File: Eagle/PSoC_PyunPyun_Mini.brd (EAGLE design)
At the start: 57.1 x 52.1 mm, 26 parts, among them IC1 NJM2732

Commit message: change Bord Design
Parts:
- moved R3 2.54 mm to (33.0, 16.5)
- moved JP9 2.54 mm to (38.1, 22.9)
- moved R5 2.54 mm to (29.2, 10.2)
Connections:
- net IDAC7: now also JP3.9; no longer JP3.8
- net IDAC8: now also JP3.8; no longer JP3.9
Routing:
- net AGND: track 65.6 -> 72.2 mm
- net +3.3V: track 44.8 -> 50.8 mm
- net GND: track 93.5 -> 88.9 mm
- net +5V: track 56.4 -> 61.0 mm
- net RST: track 32.6 -> 35.6 mm
- net N$2: track 25.0 -> 27.9 mm
- net N$1: track 12.7 -> 10.2 mm
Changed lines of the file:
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@@
 <element name="R13" library="rcl" package="0207/7" value="1k" x="44.45" y="35.56"/>
 <element name="R2" library="rcl" package="0207/7" value="33k" x="27.94" y="16.51" rot="R90"/>
-<element name="R3" library="rcl" package="0207/7" value="2.2k" x="33.02" y="13.97" rot="R270"/>
+<element name="R3" library="rcl" package="0207/7" value="2.2k" x="33.02" y="16.51" rot="R270"/>
 <element name="R4" library="rcl" package="0207/7" value="10k" x="15.24" y="26.67" rot="R90"/>
 <element name="R9" library="rcl" package="0207/7" value="10k" x="27.94" y="36.83" rot="R90"/>
@@
 <element name="IC1" library="linear" package="DIL08" value="NJM2732" x="24.13" y="26.67"/>
 <element name="JP7" library="pinhead" package="1X02" value="RCA_GND" x="13.97" y="20.32" rot="R180"/>
-<element name="R5" library="rcl" package="0207/7" value="10k" x="26.67" y="10.16" rot="R180"/>
+<element name="R5" library="rcl" package="0207/7" value="10k" x="29.21" y="10.16" rot="R180"/>
 <element name="C4" library="rcl" package="C050-024X044" value="1500pF" x="30.48" y="15.24" rot="R90"/>
 <element name="JP8" library="pinhead" package="1X01" value="TP-VGND" x="15.24" y="15.24" rot="R180"/>
-<element name="JP9" library="pinhead" package="1X01" value="TP-GND" x="38.1" y="20.32"/>
+<element name="JP9" library="pinhead" package="1X01" value="TP-GND" x="38.1" y="22.86"/>
 <element name="JP4" library="pinhead" package="1X09" value="" x="50.8" y="25.4" rot="R90"/>
 </elements>
@@
 <contactref element="R2" pad="1"/>
 <contactref element="C2" pad="1"/>
-<wire x1="20.32" y1="12.7" x2="20.32" y2="15.24" width="0.4064" layer="16"/>
-<wire x1="20.32" y1="15.24" x2="22.86" y2="15.24" width="0.4064" layer="16"/>
 <wire x1="22.86" y1="15.24" x2="22.86" y2="12.7" width="0.4064" layer="16"/>
 <wire x1="22.86" y1="12.7" x2="27.94" y2="12.7" width="0.4064" layer="16"/>
+<wire x1="20.32" y1="12.7" x2="22.86" y2="12.7" width="0.4064" layer="16"/>
 </signal>
 <signal name="IDAC8">
-<contactref element="JP3" pad="9"/>
 <contactref element="R5" pad="1"/>
 <contactref element="R3" pad="2"/>
-<wire x1="33.02" y1="10.16" x2="30.48" y2="10.16" width="0.4064" layer="16"/>
-<wire x1="30.48" y1="10.16" x2="30.48" y2="5.08" width="0.4064" layer="16"/>
+<wire x1="33.02" y1="12.7" x2="33.02" y2="10.16" width="0.4064" layer="16"/>
+<contactref element="JP3" pad="8"/>
+<wire x1="33.02" y1="5.08" x2="33.02" y2="10.16" width="0.4064" layer="16"/>
 </signal>
 <signal name="N$3">
@@
 <wire x1="27.94" y1="22.86" x2="30.48" y2="22.86" width="0.4064" layer="16"/>
 <wire x1="25.4" y1="48.26" x2="25.4" y2="35.56" width="0.4064" layer="16"/>
-<wire x1="35.56" y1="35.56" x2="38.1" y2="33.02" width="0.4064" layer="16"/>
-<wire x1="38.1" y1="33.02" x2="38.1" y2="20.32" width="0.4064" layer="16"/>
+<wire x1="38.1" y1="35.56" x2="38.1" y2="22.86" width="0.4064" layer="16"/>
 <wire x1="25.4" y1="35.56" x2="35.56" y2="35.56" width="0.4064" layer="16"/>
-<wire x1="30.48" y1="22.86" x2="33.02" y2="20.32" width="0.4064" layer="16"/>
-<wire x1="33.02" y1="20.32" x2="38.1" y2="20.32" width="0.4064" layer="16"/>
 <contactref element="JP4" pad="4"/>
 <contactref element="JP4" pad="8"/>
 <wire x1="50.8" y1="33.02" x2="43.18" y2="33.02" width="0.4064" layer="16"/>
-<wire x1="43.18" y1="33.02" x2="43.18" y2="20.32" width="0.4064" layer="16"/>
-<wire x1="43.18" y1="20.32" x2="38.1" y2="20.32" width="0.4064" layer="16"/>
+<wire x1="43.18" y1="33.02" x2="43.18" y2="22.86" width="0.4064" layer="16"/>
+<wire x1="43.18" y1="22.86" x2="38.1" y2="22.86" width="0.4064" layer="16"/>
 <wire x1="50.8" y1="22.86" x2="54.61" y2="22.86" width="0.4064" layer="1"/>
 <wire x1="54.61" y1="22.86" x2="54.61" y2="33.02" width="0.4064" layer="1"/>
 <wire x1="54.61" y1="33.02" x2="50.8" y2="33.02" width="0.4064" layer="1"/>
+<wire x1="30.48" y1="22.86" x2="38.1" y2="22.86" width="0.4064" layer="16"/>
+<wire x1="35.56" y1="35.56" x2="38.1" y2="35.56" width="0.4064" layer="16"/>
 </signal>
 <signal name="N$8">
@@
 <contactref element="IC1" pad="8"/>
 <wire x1="17.78" y1="30.48" x2="20.32" y2="30.48" width="0.4064" layer="16"/>
-<wire x1="35.56" y1="25.4" x2="24.13" y2="25.4" width="0.4064" layer="1"/>
-<wire x1="24.13" y1="25.4" x2="20.32" y2="29.21" width="0.4064" layer="1"/>
-<wire x1="20.32" y1="29.21" x2="20.32" y2="30.48" width="0.4064" layer="1"/>
-<wire x1="20.32" y1="30.48" x2="20.32" y2="33.02" width="0.4064" layer="1"/>
-<wire x1="20.32" y1="33.02" x2="27.94" y2="40.64" width="0.4064" layer="1"/>
-<wire x1="40.64" y1="35.56" x2="35.56" y2="40.64" width="0.4064" layer="16"/>
-<wire x1="35.56" y1="40.64" x2="30.48" y2="40.64" width="0.4064" layer="16"/>
+<wire x1="40.64" y1="35.56" x2="40.64" y2="40.64" width="0.4064" layer="16"/>
+<wire x1="40.64" y1="40.64" x2="30.48" y2="40.64" width="0.4064" layer="16"/>
 <wire x1="30.48" y1="40.64" x2="27.94" y2="40.64" width="0.4064" layer="16"/>
 <wire x1="30.48" y1="48.26" x2="30.48" y2="40.64" width="0.4064" layer="16"/>
+<wire x1="27.94" y1="40.64" x2="20.32" y2="40.64" width="0.4064" layer="1"/>
+<wire x1="20.32" y1="40.64" x2="20.32" y2="30.48" width="0.4064" layer="1"/>
+<wire x1="35.56" y1="25.4" x2="40.64" y2="25.4" width="0.4064" layer="1"/>
+<wire x1="40.64" y1="25.4" x2="40.64" y2="35.56" width="0.4064" layer="1"/>
 </signal>
 <signal name="AGND">
@@
 <wire x1="15.24" y1="22.86" x2="15.24" y2="20.32" width="0.4064" layer="16"/>
 <wire x1="25.4" y1="30.48" x2="22.86" y2="30.48" width="0.4064" layer="16"/>
-<wire x1="33.02" y1="17.78" x2="30.48" y2="17.78" width="0.4064" layer="16"/>
 <wire x1="15.24" y1="15.24" x2="16.51" y2="16.51" width="0.4064" layer="1"/>
 <wire x1="16.51" y1="16.51" x2="24.13" y2="16.51" width="0.4064" layer="1"/>
 <wire x1="24.13" y1="16.51" x2="25.4" y2="15.24" width="0.4064" layer="1"/>
 <wire x1="15.24" y1="20.32" x2="15.24" y2="15.24" width="0.4064" layer="16"/>
-<wire x1="25.4" y1="15.24" x2="27.94" y2="17.78" width="0.4064" layer="16"/>
-<wire x1="27.94" y1="17.78" x2="30.48" y2="17.78" width="0.4064" layer="16"/>
 <wire x1="15.24" y1="22.86" x2="15.24" y2="25.4" width="0.4064" layer="16"/>
 <wire x1="15.24" y1="25.4" x2="15.24" y2="27.94" width="0.4064" layer="16"/>
@@
 <wire x1="35.56" y1="27.94" x2="30.48" y2="27.94" width="0.4064" layer="16"/>
 <wire x1="35.56" y1="27.94" x2="35.56" y2="33.02" width="0.4064" layer="16"/>
+<wire x1="25.4" y1="15.24" x2="33.02" y2="15.24" width="0.4064" layer="16"/>
+<wire x1="33.02" y1="15.24" x2="33.02" y2="17.78" width="0.4064" layer="16"/>
+<wire x1="33.02" y1="17.78" x2="33.02" y2="20.32" width="0.4064" layer="16"/>
+<wire x1="30.48" y1="17.78" x2="33.02" y2="17.78" width="0.4064" layer="16"/>
 </signal>
 <signal name="+3.3V">
 <contactref element="JP1" pad="4"/>
 <contactref element="JP4" pad="1"/>
-<wire x1="50.8" y1="15.24" x2="43.18" y2="15.24" width="0.4064" layer="1"/>
-<wire x1="43.18" y1="15.24" x2="40.64" y2="17.78" width="0.4064" layer="1"/>
-<wire x1="33.02" y1="48.26" x2="33.02" y2="40.64" width="0.4064" layer="1"/>
-<wire x1="33.02" y1="40.64" x2="40.64" y2="33.02" width="0.4064" layer="1"/>
-<wire x1="40.64" y1="33.02" x2="40.64" y2="17.78" width="0.4064" layer="1"/>
+<wire x1="50.8" y1="15.24" x2="46.99" y2="15.24" width="0.4064" layer="1"/>
+<wire x1="46.99" y1="15.24" x2="46.99" y2="41.91" width="0.4064" layer="1"/>
+<wire x1="46.99" y1="41.91" x2="33.02" y2="41.91" width="0.4064" layer="1"/>
+<wire x1="33.02" y1="41.91" x2="33.02" y2="48.26" width="0.4064" layer="1"/>
 </signal>
 <signal name="RST">
 <contactref element="JP3" pad="5"/>
 <contactref element="JP4" pad="7"/>
-<wire x1="40.64" y1="5.08" x2="40.64" y2="12.7" width="0.4064" layer="16"/>
-<wire x1="40.64" y1="12.7" x2="45.72" y2="17.78" width="0.4064" layer="16"/>
-<wire x1="45.72" y1="17.78" x2="45.72" y2="30.48" width="0.4064" layer="16"/>
+<wire x1="40.64" y1="5.08" x2="40.64" y2="20.32" width="0.4064" layer="16"/>
+<wire x1="40.64" y1="20.32" x2="45.72" y2="20.32" width="0.4064" layer="16"/>
+<wire x1="45.72" y1="20.32" x2="45.72" y2="30.48" width="0.4064" layer="16"/>
 <wire x1="45.72" y1="30.48" x2="50.8" y2="30.48" width="0.4064" layer="16"/>
 </signal>
@@
 <contactref element="R1" pad="1"/>
 <contactref element="C4" pad="1"/>
-<wire x1="20.32" y1="20.32" x2="17.78" y2="17.78" width="0.4064" layer="16"/>
-<wire x1="17.78" y1="17.78" x2="17.78" y2="10.16" width="0.4064" layer="16"/>
-<wire x1="17.78" y1="10.16" x2="22.86" y2="10.16" width="0.4064" layer="16"/>
-<wire x1="30.48" y1="12.7" x2="27.94" y2="10.16" width="0.4064" layer="16"/>
-<wire x1="27.94" y1="10.16" x2="22.86" y2="10.16" width="0.4064" layer="16"/>
+<wire x1="25.4" y1="10.16" x2="17.78" y2="10.16" width="0.4064" layer="16"/>
+<wire x1="17.78" y1="10.16" x2="17.78" y2="20.32" width="0.4064" layer="16"/>
+<wire x1="17.78" y1="20.32" x2="20.32" y2="20.32" width="0.4064" layer="16"/>
+<wire x1="25.4" y1="10.16" x2="30.48" y2="10.16" width="0.4064" layer="16"/>
+<wire x1="30.48" y1="10.16" x2="30.48" y2="12.7" width="0.4064" layer="16"/>
 </signal>
 <signal name="IDAC7">
-<contactref element="JP3" pad="8"/>
+<contactref element="JP3" pad="9"/>
 </signal>
 </signals>

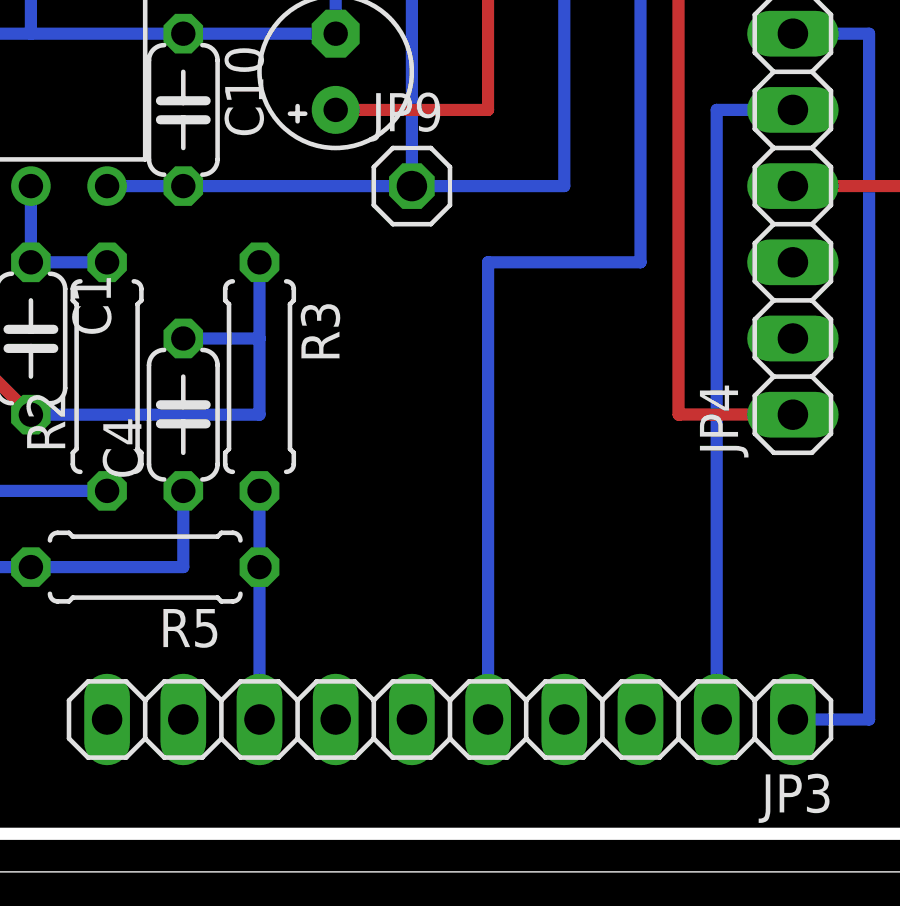
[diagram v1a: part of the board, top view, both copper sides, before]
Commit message: 回路図・基板図 RST信号に抵抗分圧を追加
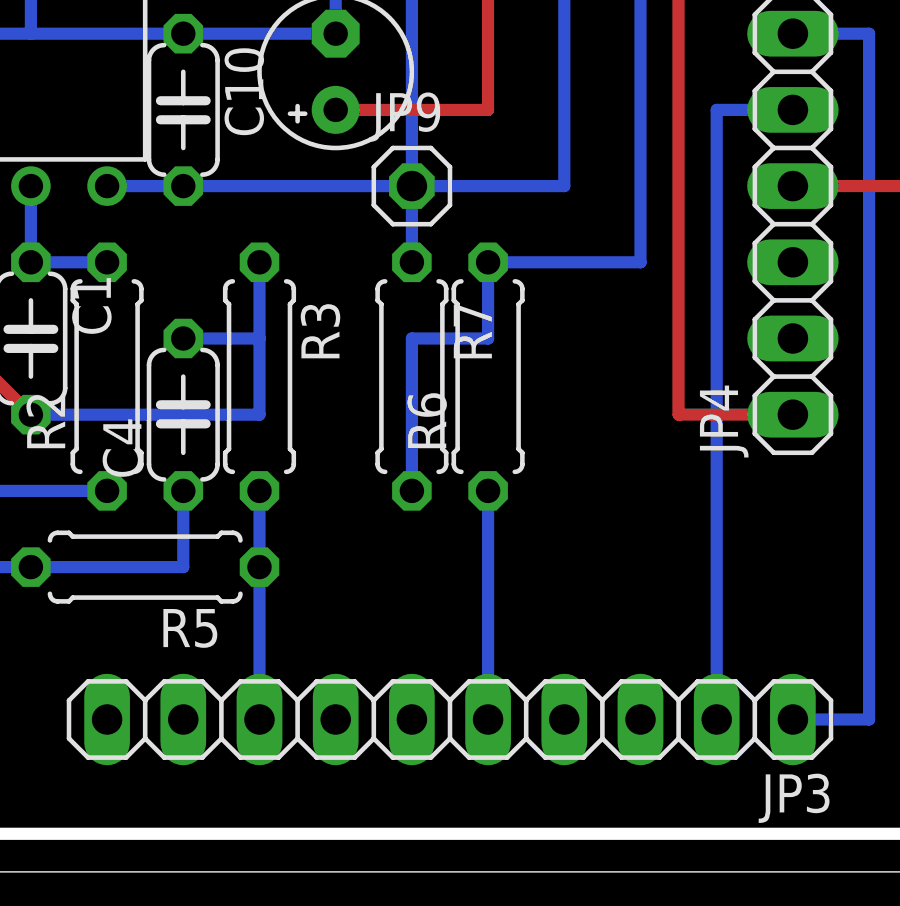
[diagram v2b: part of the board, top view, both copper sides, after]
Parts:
- added R6: 1.2k, rcl:0207/7
- added R7: 2.2k, rcl:0207/7
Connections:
- new net N$6: JP3.5, R6.1
- net GND: now also R7.1
- net RST: now also R6.2, R7.2; no longer JP3.5
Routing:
- net N$6: track 0.00 -> 7.62 mm
- net RST: track 35.6 -> 30.5 mm
- net GND: track 88.9 -> 91.4 mm
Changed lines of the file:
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@@
 <element name="JP9" library="pinhead" package="1X01" value="TP-GND" x="38.1" y="22.86"/>
 <element name="JP4" library="pinhead" package="1X09" value="" x="50.8" y="25.4" rot="R90"/>
+<element name="R6" library="rcl" package="0207/7" value="1.2k" x="40.64" y="16.51" rot="R90"/>
+<element name="R7" library="rcl" package="0207/7" value="2.2k" x="38.1" y="16.51" rot="R270"/>
 </elements>
 <signals>
@@
 <wire x1="30.48" y1="22.86" x2="38.1" y2="22.86" width="0.4064" layer="16"/>
 <wire x1="35.56" y1="35.56" x2="38.1" y2="35.56" width="0.4064" layer="16"/>
+<contactref element="R7" pad="1"/>
+<wire x1="38.1" y1="20.32" x2="38.1" y2="22.86" width="0.4064" layer="16"/>
 </signal>
 <signal name="N$8">
@@
 </signal>
 <signal name="RST">
-<contactref element="JP3" pad="5"/>
 <contactref element="JP4" pad="7"/>
-<wire x1="40.64" y1="5.08" x2="40.64" y2="20.32" width="0.4064" layer="16"/>
-<wire x1="40.64" y1="20.32" x2="45.72" y2="20.32" width="0.4064" layer="16"/>
 <wire x1="45.72" y1="20.32" x2="45.72" y2="30.48" width="0.4064" layer="16"/>
 <wire x1="45.72" y1="30.48" x2="50.8" y2="30.48" width="0.4064" layer="16"/>
+<contactref element="R6" pad="2"/>
+<contactref element="R7" pad="2"/>
+<wire x1="40.64" y1="20.32" x2="45.72" y2="20.32" width="0.4064" layer="16"/>
+<wire x1="38.1" y1="12.7" x2="38.1" y2="17.78" width="0.4064" layer="16"/>
+<wire x1="38.1" y1="17.78" x2="40.64" y2="17.78" width="0.4064" layer="16"/>
+<wire x1="40.64" y1="17.78" x2="40.64" y2="20.32" width="0.4064" layer="16"/>
 </signal>
 <signal name="SCL">
@@
 <contactref element="JP3" pad="9"/>
 </signal>
+<signal name="N$6">
+<contactref element="JP3" pad="5"/>
+<contactref element="R6" pad="1"/>
+<wire x1="40.64" y1="12.7" x2="40.64" y2="5.08" width="0.4064" layer="16"/>
+</signal>
 </signals>

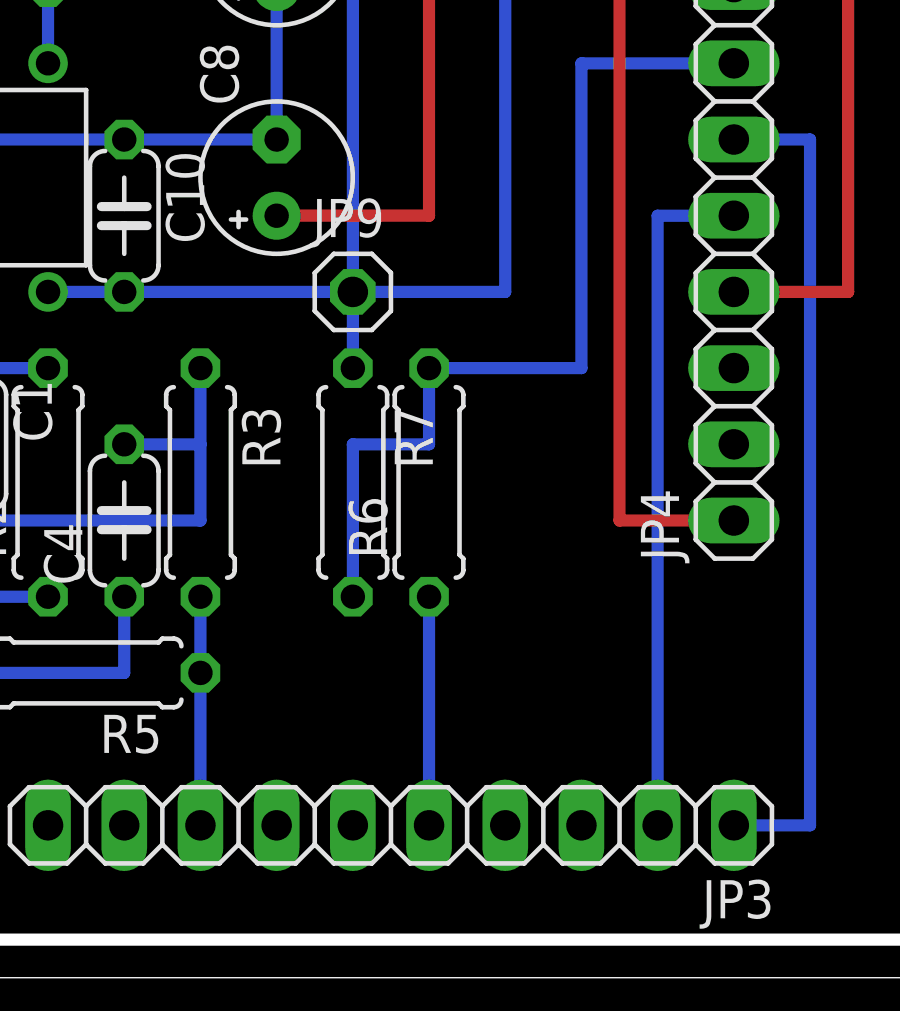
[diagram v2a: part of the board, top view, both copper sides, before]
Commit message: 基板設計図 RST信号の分圧抵抗の位置を変更
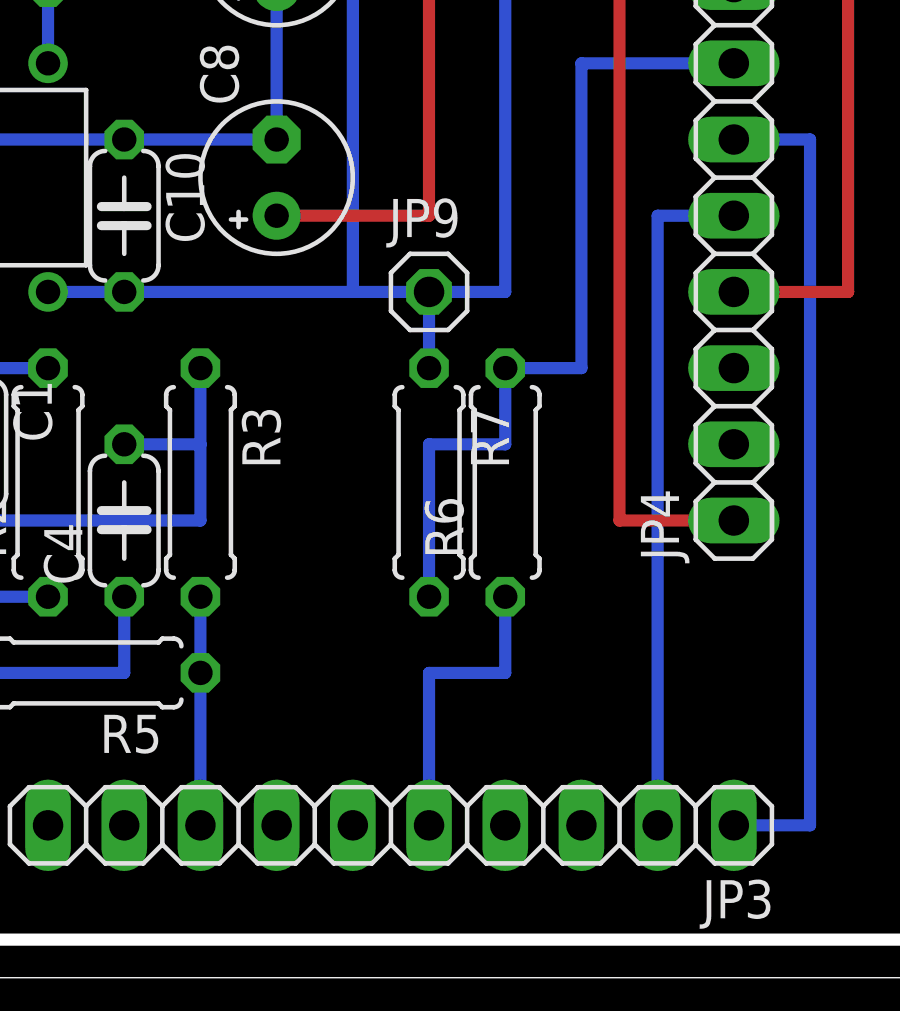
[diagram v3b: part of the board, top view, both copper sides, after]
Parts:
- moved JP9 2.54 mm to (40.6, 22.9)
- moved R6 2.54 mm to (43.2, 16.5)
- moved R7 2.54 mm to (40.6, 16.5)
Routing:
- net RST: track 30.5 -> 27.9 mm
- net N$6: track 7.62 -> 10.2 mm
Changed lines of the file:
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@@
 <element name="C4" library="rcl" package="C050-024X044" value="1500pF" x="30.48" y="15.24" rot="R90"/>
 <element name="JP8" library="pinhead" package="1X01" value="TP-VGND" x="15.24" y="15.24" rot="R180"/>
-<element name="JP9" library="pinhead" package="1X01" value="TP-GND" x="38.1" y="22.86"/>
+<element name="JP9" library="pinhead" package="1X01" value="TP-GND" x="40.64" y="22.86"/>
 <element name="JP4" library="pinhead" package="1X09" value="" x="50.8" y="25.4" rot="R90"/>
-<element name="R6" library="rcl" package="0207/7" value="1.2k" x="40.64" y="16.51" rot="R90"/>
-<element name="R7" library="rcl" package="0207/7" value="2.2k" x="38.1" y="16.51" rot="R270"/>
+<element name="R6" library="rcl" package="0207/7" value="1.2k" x="43.18" y="16.51" rot="R90"/>
+<element name="R7" library="rcl" package="0207/7" value="2.2k" x="40.64" y="16.51" rot="R270"/>
 </elements>
 <signals>
@@
 <wire x1="27.94" y1="22.86" x2="30.48" y2="22.86" width="0.4064" layer="16"/>
 <wire x1="25.4" y1="48.26" x2="25.4" y2="35.56" width="0.4064" layer="16"/>
-<wire x1="38.1" y1="35.56" x2="38.1" y2="22.86" width="0.4064" layer="16"/>
 <wire x1="25.4" y1="35.56" x2="35.56" y2="35.56" width="0.4064" layer="16"/>
 <contactref element="JP4" pad="4"/>
@@
 <wire x1="50.8" y1="33.02" x2="43.18" y2="33.02" width="0.4064" layer="16"/>
 <wire x1="43.18" y1="33.02" x2="43.18" y2="22.86" width="0.4064" layer="16"/>
-<wire x1="43.18" y1="22.86" x2="38.1" y2="22.86" width="0.4064" layer="16"/>
+<wire x1="43.18" y1="22.86" x2="40.64" y2="22.86" width="0.4064" layer="16"/>
 <wire x1="50.8" y1="22.86" x2="54.61" y2="22.86" width="0.4064" layer="1"/>
 <wire x1="54.61" y1="22.86" x2="54.61" y2="33.02" width="0.4064" layer="1"/>
 <wire x1="54.61" y1="33.02" x2="50.8" y2="33.02" width="0.4064" layer="1"/>
 <wire x1="30.48" y1="22.86" x2="38.1" y2="22.86" width="0.4064" layer="16"/>
+<wire x1="38.1" y1="22.86" x2="40.64" y2="22.86" width="0.4064" layer="16"/>
 <wire x1="35.56" y1="35.56" x2="38.1" y2="35.56" width="0.4064" layer="16"/>
 <contactref element="R7" pad="1"/>
-<wire x1="38.1" y1="20.32" x2="38.1" y2="22.86" width="0.4064" layer="16"/>
+<wire x1="40.64" y1="20.32" x2="40.64" y2="22.86" width="0.4064" layer="16"/>
+<wire x1="38.1" y1="35.56" x2="38.1" y2="22.86" width="0.4064" layer="16"/>
 </signal>
 <signal name="N$8">
@@
 <contactref element="R6" pad="2"/>
 <contactref element="R7" pad="2"/>
-<wire x1="40.64" y1="20.32" x2="45.72" y2="20.32" width="0.4064" layer="16"/>
-<wire x1="38.1" y1="12.7" x2="38.1" y2="17.78" width="0.4064" layer="16"/>
-<wire x1="38.1" y1="17.78" x2="40.64" y2="17.78" width="0.4064" layer="16"/>
-<wire x1="40.64" y1="17.78" x2="40.64" y2="20.32" width="0.4064" layer="16"/>
+<wire x1="43.18" y1="20.32" x2="45.72" y2="20.32" width="0.4064" layer="16"/>
+<wire x1="40.64" y1="12.7" x2="40.64" y2="17.78" width="0.4064" layer="16"/>
+<wire x1="40.64" y1="17.78" x2="43.18" y2="17.78" width="0.4064" layer="16"/>
+<wire x1="43.18" y1="17.78" x2="43.18" y2="20.32" width="0.4064" layer="16"/>
 </signal>
 <signal name="SCL">
@@
 <contactref element="JP3" pad="5"/>
 <contactref element="R6" pad="1"/>
-<wire x1="40.64" y1="12.7" x2="40.64" y2="5.08" width="0.4064" layer="16"/>
+<wire x1="40.64" y1="5.08" x2="40.64" y2="10.16" width="0.4064" layer="16"/>
+<wire x1="40.64" y1="10.16" x2="43.18" y2="10.16" width="0.4064" layer="16"/>
+<wire x1="43.18" y1="10.16" x2="43.18" y2="12.7" width="0.4064" layer="16"/>
 </signal>
 </signals>
